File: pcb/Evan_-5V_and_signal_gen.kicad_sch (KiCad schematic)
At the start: 34 parts, among them IC1 TL7660IDGKR, IC2 TL081IDT, IC4 UA78M33CDCYG3, IC9 TL081IDT, U5 TPS2069CDBVR_MOSFET

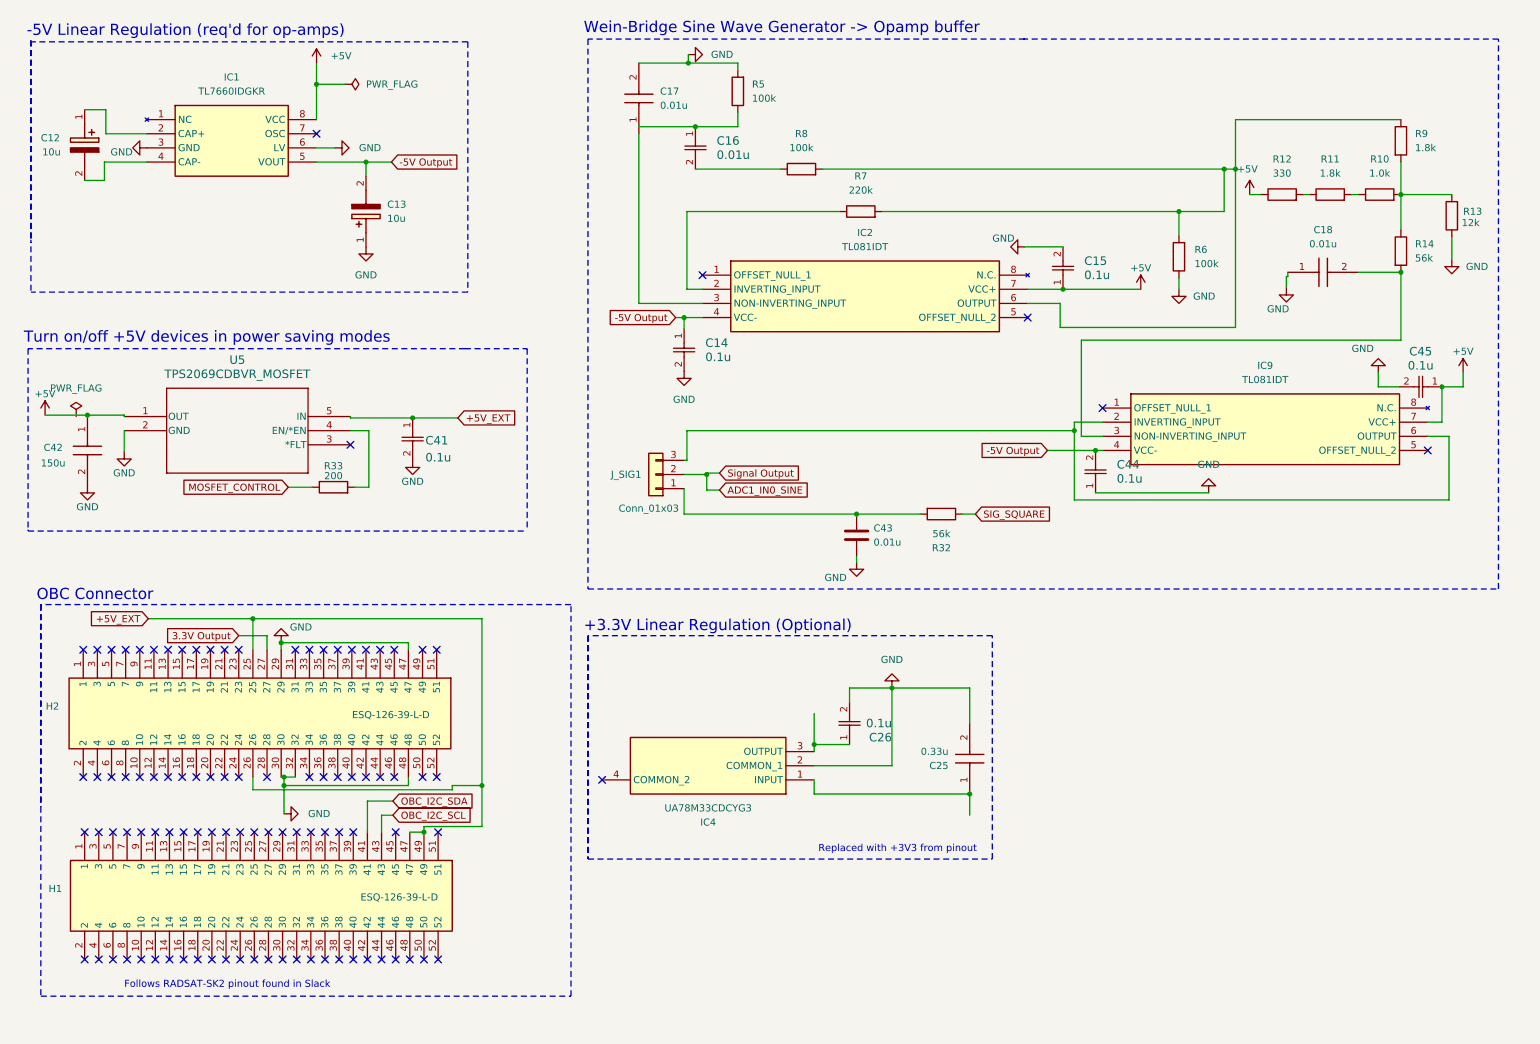
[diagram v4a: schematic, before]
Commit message: Added RC Ladder Circuit
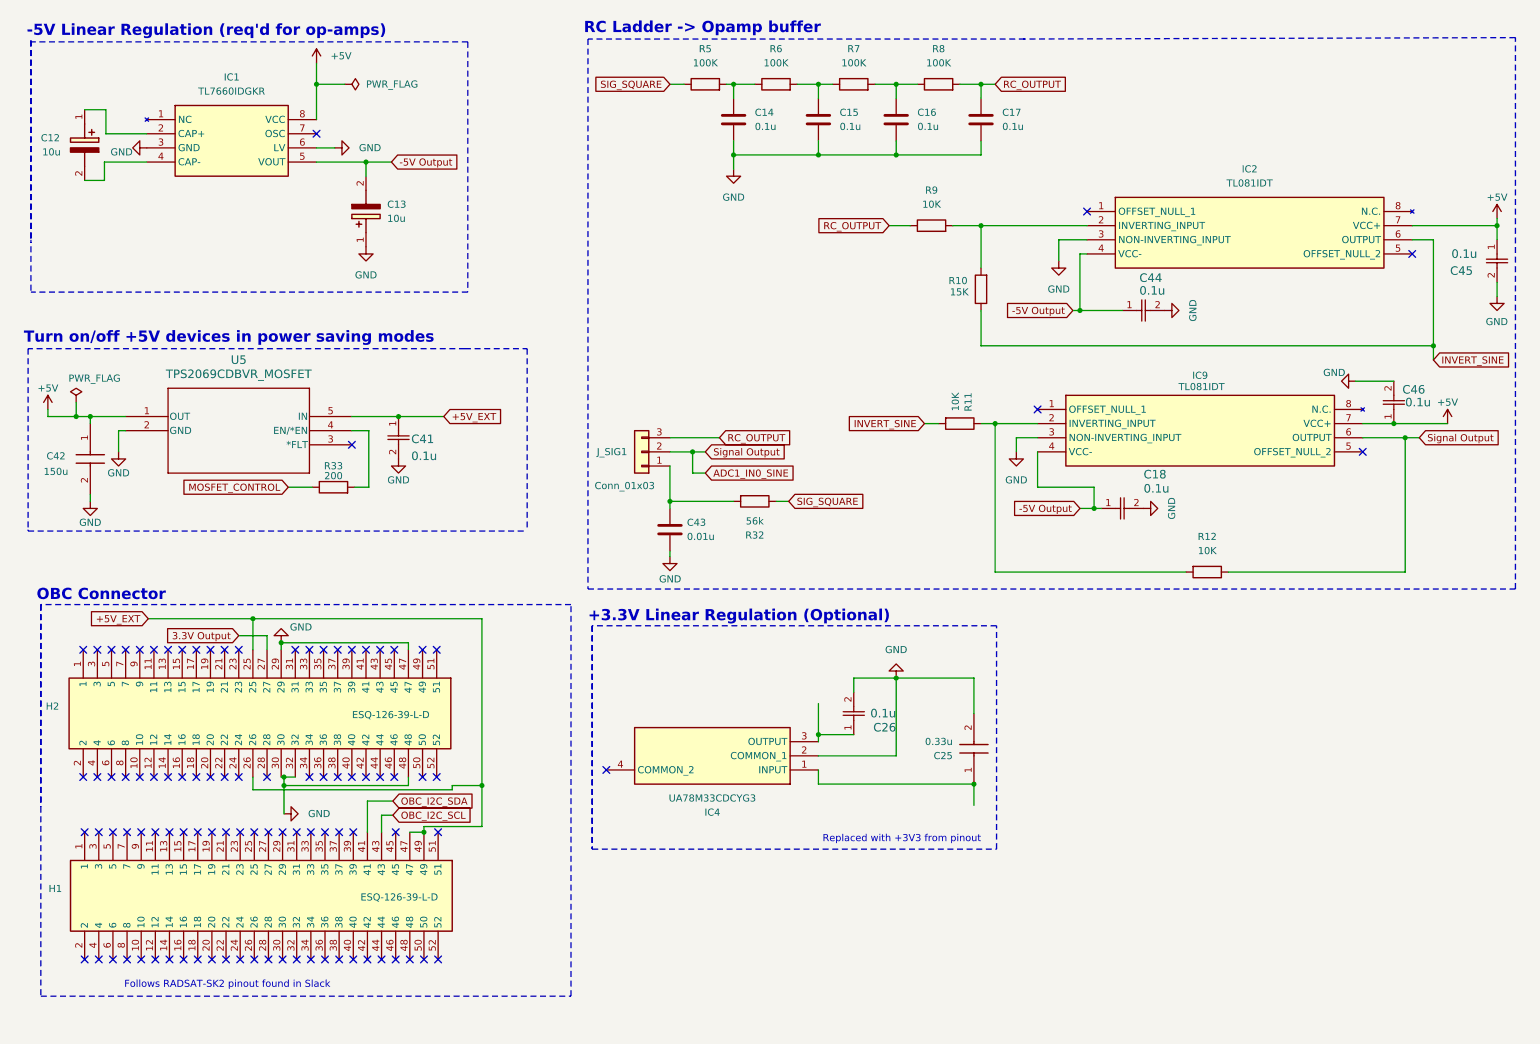
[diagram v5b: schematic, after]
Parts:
- removed C14, C15: 0.1u, capstone:CAPC220145_88N_KEM-0.1u, symbol capstone:C0805C104K5RAC7210
- removed C16: 0.01u, capstone:CAPC220145_88N_KEM-0.1u, symbol capstone:C0805C104K5RAC7210
- removed C17, C18: 0.01u, capstone:C0805, symbol capstone:C0805C103F5GACTU
- removed R13: 12k, Resistor_SMD:R_0402_1005Metric, symbol Device:R
- removed R14: 56k, Resistor_SMD:R_0402_1005Metric, symbol Device:R
- added C14, C15, C16, C17: 0.1u, capstone:CAPC220145_88N_KEM-0.1u, symbol Device:C
- added C18, C46: 0.1u, capstone:CAPC220145_88N_KEM-0.1u, symbol capstone:C0805C104K5RAC7210
- IC2, IC9: footprint capstone:SOIC127P600X175-8N -> SOIC127P600X175-8N
- R10: value 1.0k -> 15K; footprint Resistor_SMD:R_0402_1005Metric -> (none)
- R11, R9: value 1.8k -> 10K; footprint Resistor_SMD:R_0402_1005Metric -> (none)
- R12: value 330 -> 10K; footprint Resistor_SMD:R_0402_1005Metric -> (none)
- R5, R6, R8: value 100k -> 100K
- R7: value 220k -> 100K
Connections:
- net +5V: now also C46.1; no longer R12.1
- net -5V Output: now also C44.1, C18.1; no longer C44.2
- net ADC1_IN0_SINE: now also IC9.6 (OUTPUT), R12.1
- net GND: now also C44.2, IC2.3 (NON-INVERTING_INPUT), IC9.3 (NON-INVERTING_INPUT), C14.2, C15.2, C16.2, C17.2, C18.2, C46.2; no longer C44.1, R5.2, R6.1
- net SIG_SQUARE: now also R5.1
- net at R11.1, R12.2: now also IC9.2 (INVERTING_INPUT)
- net INVERT_SINE: now reaches R10.1, R11.2
- net INVERT_SINE: now also IC2.6 (OUTPUT)
- net at IC2.2 (INVERTING_INPUT): now also R10.2, R9.2; no longer R7.1
- net at R8.1: now also R7.2, C16.1
- new net: C15.1, R6.2, R7.1
- new net: C14.1, R5.2, R6.1
- new net RC_OUTPUT: C17.1, J_SIG1.3 (Pin_3), R8.2, R9.1
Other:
- note added: "RC Ladder -> Opamp buffer"
- note removed: "Wein-Bridge Sine Wave Generator -> Opamp buffer"
- moved on the sheet: C25, C26, C41, C42, C43, IC4, J_SIG1, R32

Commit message: Routed all RC ladder connections
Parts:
- IC2, IC9: footprint SOIC127P600X175-8N -> capstone:SOIC127P600X175-8N
- R10, R11, R12, R9: footprint (none) -> Resistor_SMD:R_0402_1005Metric
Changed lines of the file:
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@@
 			)
 		)
-		(property "Footprint" "SOIC127P600X175-8N"
+		(property "Footprint" "capstone:SOIC127P600X175-8N"
 			(at 261.62 143.18 0)
 			(effects
@@
 			)
 		)
-		(property "Footprint" ""
+		(property "Footprint" "Resistor_SMD:R_0402_1005Metric"
 			(at 228.6 111.252 90)
 			(effects
@@
 			)
 		)
-		(property "Footprint" ""
+		(property "Footprint" "Resistor_SMD:R_0402_1005Metric"
 			(at 179.07 52.578 90)
 			(effects
@@
 			)
 		)
-		(property "Footprint" ""
+		(property "Footprint" "Resistor_SMD:R_0402_1005Metric"
 			(at 184.15 84.582 90)
 			(effects
@@
 			)
 		)
-		(property "Footprint" "SOIC127P600X175-8N"
+		(property "Footprint" "capstone:SOIC127P600X175-8N"
 			(at 252.73 178.74 0)
 			(effects
@@
 			)
 		)
-		(property "Footprint" ""
+		(property "Footprint" "Resistor_SMD:R_0402_1005Metric"
 			(at 189.738 62.23 90)
 			(effects

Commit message: Added reset button & LED, fixed SD card overhang
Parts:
- C14, C15, C16, C17: value 0.1u -> 0.01u
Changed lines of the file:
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@@
 			)
 		)
-		(property "Value" "0.1u"
+		(property "Value" "0.01u"
 			(at 162.56 33.0199 0)
 			(effects
@@
 			)
 		)
-		(property "Value" "0.1u"
+		(property "Value" "0.01u"
 			(at 191.77 33.0199 0)
 			(effects
@@
 			)
 		)
-		(property "Value" "0.1u"
+		(property "Value" "0.01u"
 			(at 176.53 33.0199 0)
 			(effects
@@
 			)
 		)
-		(property "Value" "0.1u"
+		(property "Value" "0.01u"
 			(at 147.32 33.0199 0)
 			(effects

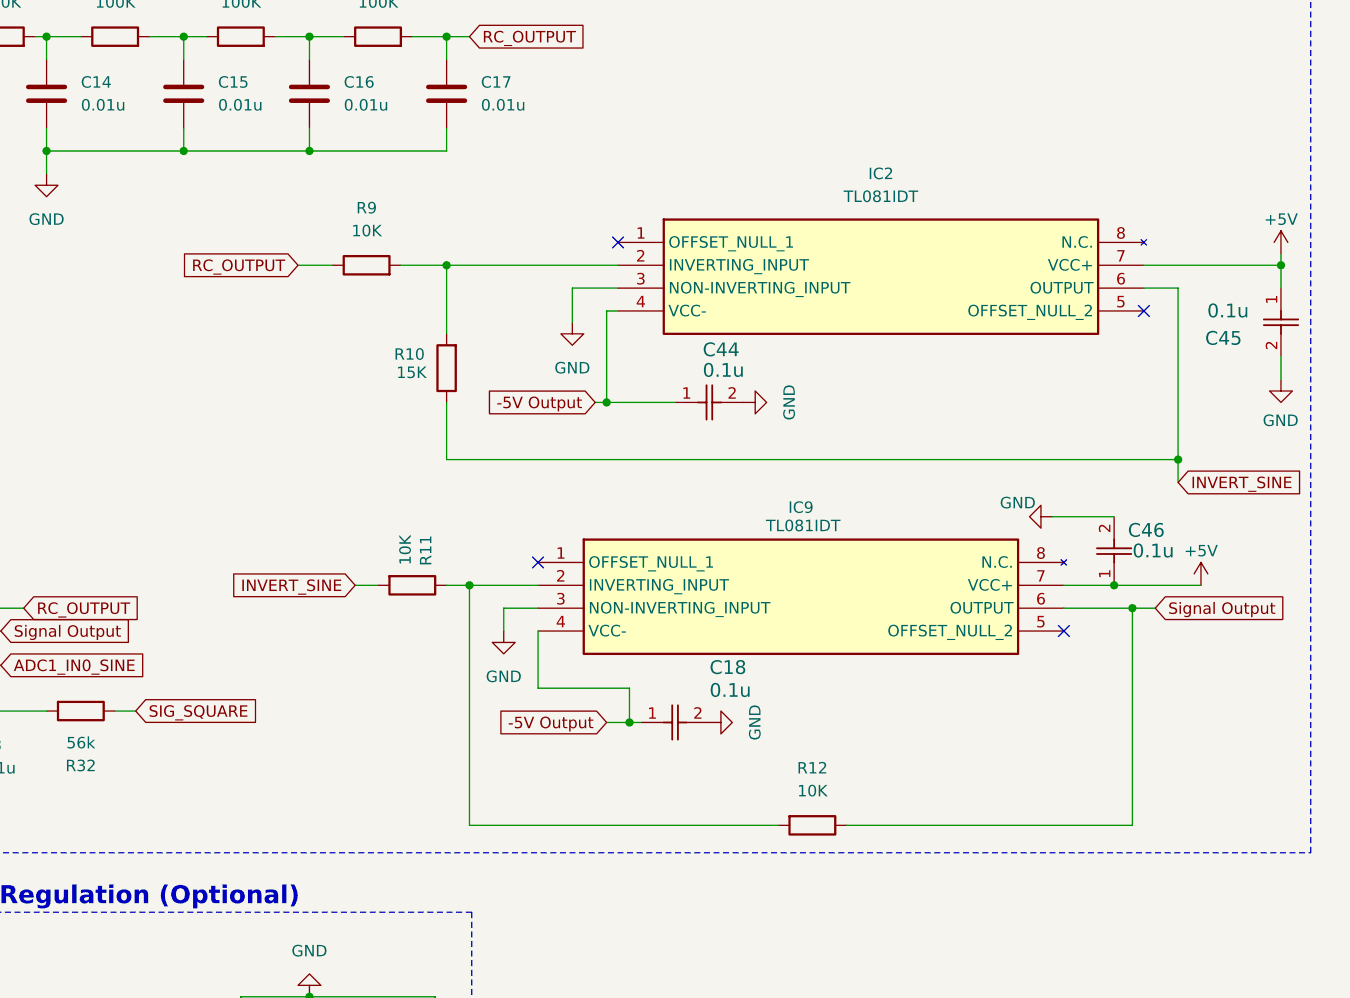
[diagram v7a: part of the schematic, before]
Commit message: Added non-inverting amplifier to RC Ladder and Changed header pin
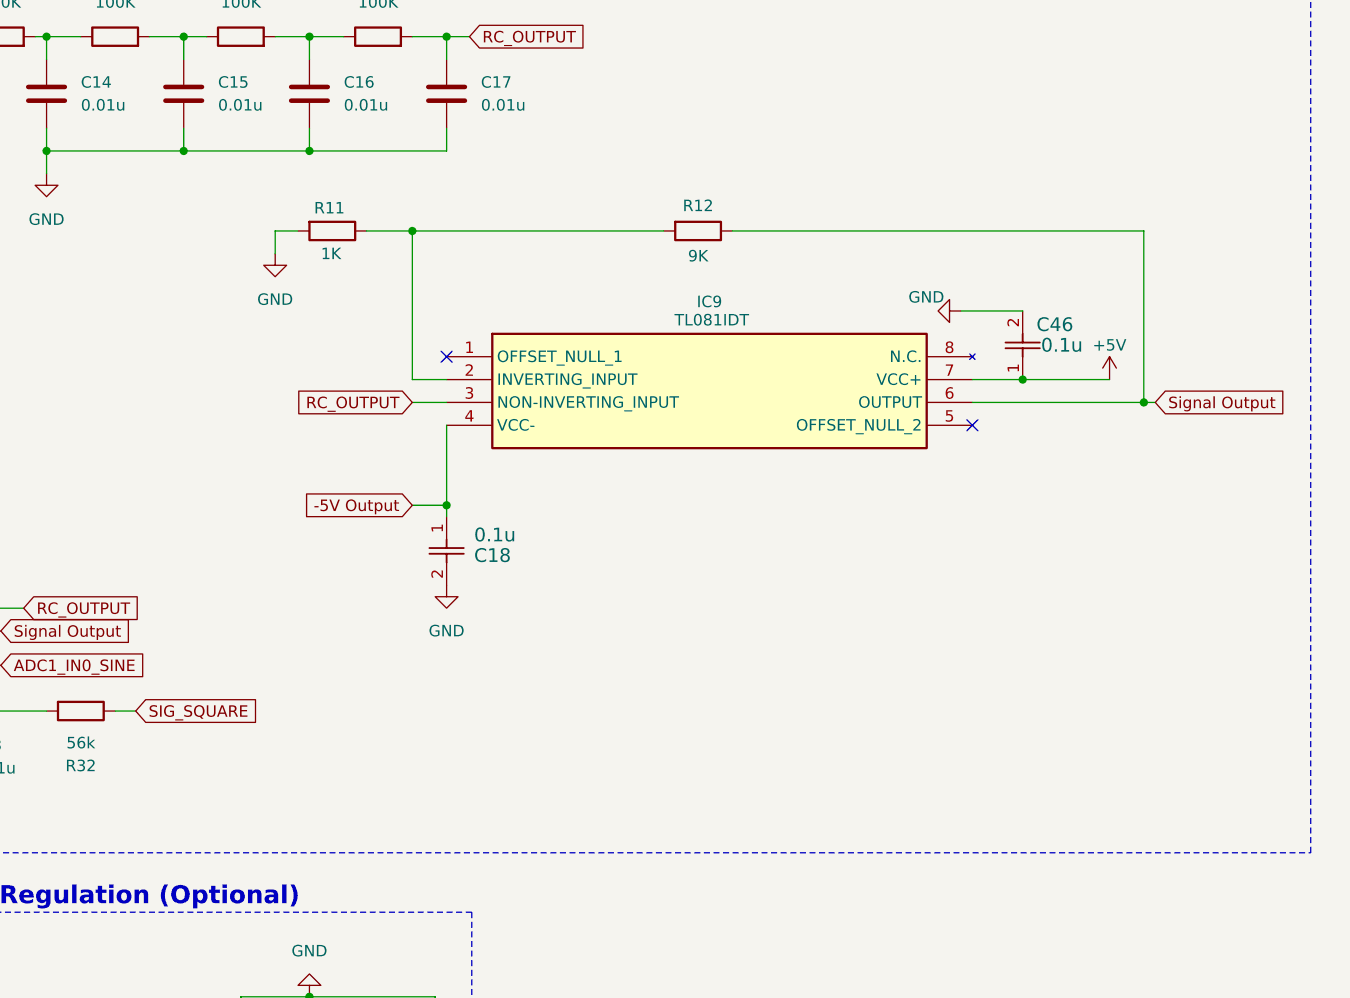
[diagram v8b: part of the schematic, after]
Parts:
- removed C44, C45: 0.1u, capstone:CAPC220145_88N_KEM-0.1u, symbol capstone:C0805C104K5RAC7210
- removed IC2: TL081IDT, capstone:SOIC127P600X175-8N, symbol capstone:TL081IDT
- removed R10: 15K, Resistor_SMD:R_0402_1005Metric, symbol Device:R
- removed R9: 10K, Resistor_SMD:R_0402_1005Metric, symbol Device:R
- R11: value 10K -> 1K
- R12: value 10K -> 9K
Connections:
- net INVERT_SINE is gone; now on net GND: R11.2
- net GND: no longer IC9.3 (NON-INVERTING_INPUT)
- net RC_OUTPUT: now also IC9.3 (NON-INVERTING_INPUT)
- no-connect marks 99 -> 97
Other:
- moved on the sheet: C18, C46, IC9, R11, R12
